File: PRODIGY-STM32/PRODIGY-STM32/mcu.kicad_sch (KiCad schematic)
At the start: 23 parts, among them U3 STM32F407VGTx, U4 M24C32-WMN6TP, Y2 8MHz, Y3 32.768kHz

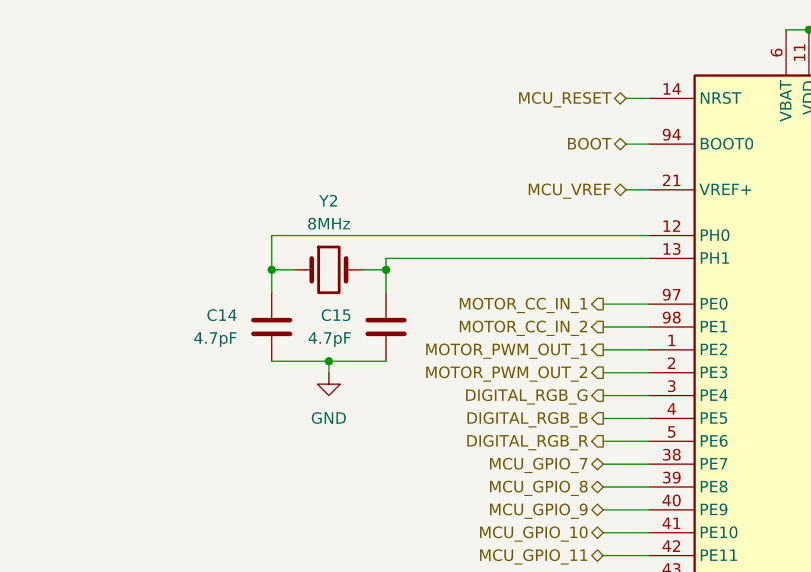
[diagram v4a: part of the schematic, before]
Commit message: stm32 started, footprints updated, lazout started
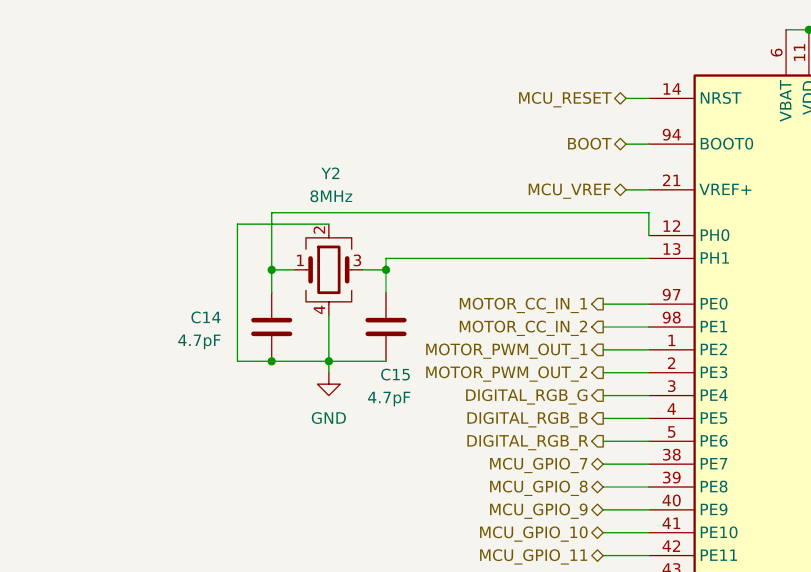
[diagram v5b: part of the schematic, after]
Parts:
- removed Y2: 8MHz, Crystal:Crystal_SMD_5032-4Pin_5.0x3.2mm, symbol Device:Crystal
- added Y2: 8MHz, Crystal:Crystal_SMD_5032-4Pin_5.0x3.2mm, symbol Device:Crystal_GND24
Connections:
- net GND: now also Y2.2, Y2.4
- net at C14.1, U3.12 (PH0): now also Y2.1
- net at C15.1, U3.13 (PH1): now also Y2.3
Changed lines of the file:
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@@
 	)
 	(junction
+		(at 59.69 60.96)
+		(diameter 0)
+		(color 0 0 0 0)
+	)
+	(junction
 		(at 224.79 62.23)
 		(diameter 0)
@@
 	(wire
 		(pts
-			(xy 59.69 46.99) (xy 101.6 46.99)
+			(xy 59.69 44.45) (xy 101.6 44.45)
 		)
 		(stroke
@@
 	(wire
 		(pts
+			(xy 55.88 60.96) (xy 59.69 60.96)
+		)
+		(stroke
+			(width 0)
+			(type default)
+		)
+	)
+	(wire
+		(pts
 			(xy 124.46 20.32) (xy 124.46 24.13)
 		)
@@
 	(wire
 		(pts
+			(xy 66.04 55.88) (xy 66.04 60.96)
+		)
+		(stroke
+			(width 0)
+			(type default)
+		)
+	)
+	(wire
+		(pts
 			(xy 157.48 167.64) (xy 151.13 167.64)
 		)
@@
 	(wire
 		(pts
+			(xy 101.6 44.45) (xy 101.6 46.99)
+		)
+		(stroke
+			(width 0)
+			(type default)
+		)
+	)
+	(wire
+		(pts
 			(xy 151.13 80.01) (xy 147.32 80.01)
 		)
@@
 	(wire
 		(pts
-			(xy 59.69 50.8) (xy 59.69 46.99)
+			(xy 59.69 50.8) (xy 59.69 44.45)
 		)
 		(stroke
@@
 	(wire
 		(pts
+			(xy 55.88 45.72) (xy 55.88 60.96)
+		)
+		(stroke
+			(width 0)
+			(type default)
+		)
+	)
+	(wire
+		(pts
 			(xy 96.52 59.69) (xy 101.6 59.69)
 		)
@@
 	(wire
 		(pts
+			(xy 66.04 45.72) (xy 55.88 45.72)
+		)
+		(stroke
+			(width 0)
+			(type default)
+		)
+	)
+	(wire
+		(pts
 			(xy 46.99 171.45) (xy 54.61 171.45)
 		)
@@
 		(dnp no)
 		(property "Reference" "C14"
-			(at 55.88 55.8799 0)
+			(at 54.102 56.134 0)
 			(effects
 				(font
@@
 		)
 		(property "Value" "4.7pF"
-			(at 55.88 58.4199 0)
+			(at 54.102 58.674 0)
 			(effects
 				(font
@@
 		)
 		(instances
-			(project ""
+			(project "PRODIGY-STM32"
 				(path "/f2f1c781-b8fe-416b-b7a0-b424640c1d9f/2c940864-b0c7-4fea-a950-c583ebb4a87f"
 					(reference "U3")
@@
 	)
 	(symbol
-		(lib_id "Device:Crystal")
-		(at 66.04 50.8 0)
-		(unit 1)
-		(exclude_from_sim no)
-		(in_bom yes)
-		(on_board yes)
-		(dnp no)
-		(fields_autoplaced yes)
-		(property "Reference" "Y2"
-			(at 66.04 43.18 0)
-			(effects
-				(font
-					(size 1.27 1.27)
-				)
-			)
-		)
-		(property "Value" "8MHz"
-			(at 66.04 45.72 0)
-			(effects
-				(font
-					(size 1.27 1.27)
-				)
-			)
-		)
-		(property "Footprint" "Crystal:Crystal_SMD_5032-4Pin_5.0x3.2mm"
-			(at 66.04 50.8 0)
-			(effects
-				(font
-					(size 1.27 1.27)
-				)
-				(hide yes)
-			)
-		)
-		(property "Datasheet" "~"
-			(at 66.04 50.8 0)
-			(effects
-				(font
-					(size 1.27 1.27)
-				)
-				(hide yes)
-			)
-		)
-		(property "Description" "Two pin crystal"
-			(at 66.04 50.8 0)
-			(effects
-				(font
-					(size 1.27 1.27)
-				)
-				(hide yes)
-			)
-		)
-		(property "MOUSER" ""
-			(at 66.04 50.8 0)
-			(effects
-				(font
-					(size 1.27 1.27)
-				)
-				(hide yes)
-			)
-		)
-		(property "TME" "8.00M-CFPX104"
-			(at 66.04 50.8 0)
-			(effects
-				(font
-					(size 1.27 1.27)
-				)
-				(hide yes)
-			)
-		)
-		(pin "1"
-		)
-		(pin "2"
-		)
-		(instances
-			(project "PRODIGY-STM32"
-				(path "/f2f1c781-b8fe-416b-b7a0-b424640c1d9f/2c940864-b0c7-4fea-a950-c583ebb4a87f"
-					(reference "Y2")
-					(unit 1)
-				)
-			)
-		)
-	)
-	(symbol
 		(lib_id "power:+3V3")
 		(at 259.08 27.94 0)
@@
 		)
 		(instances
-			(project ""
+			(project "PRODIGY-STM32"
 				(path "/f2f1c781-b8fe-416b-b7a0-b424640c1d9f/2c940864-b0c7-4fea-a950-c583ebb4a87f"
 					(reference "U4")
@@
 	)
 	(symbol
+		(lib_id "Device:Crystal_GND24")
+		(at 66.04 50.8 0)
+		(unit 1)
+		(exclude_from_sim no)
+		(in_bom yes)
+		(on_board yes)
+		(dnp no)
+		(property "Reference" "Y2"
+			(at 66.294 40.132 0)
+			(effects
+				(font
+					(size 1.27 1.27)
+				)
+			)
+		)
+		(property "Value" "8MHz"
+			(at 66.294 42.672 0)
+			(effects
+				(font
+					(size 1.27 1.27)
+				)
+			)
+		)
+		(property "Footprint" "Crystal:Crystal_SMD_5032-4Pin_5.0x3.2mm"
+			(at 66.04 50.8 0)
+			(effects
+				(font
+					(size 1.27 1.27)
+				)
+				(hide yes)
+			)
+		)
+		(property "Datasheet" "~"
+			(at 66.04 50.8 0)
+			(effects
+				(font
+					(size 1.27 1.27)
+				)
+				(hide yes)
+			)
+		)
+		(property "Description" "Four pin crystal, GND on pins 2 and 4"
+			(at 66.04 50.8 0)
+			(effects
+				(font
+					(size 1.27 1.27)
+				)
+				(hide yes)
+			)
+		)
+		(property "TME" "8.00M-CFPX104"
+			(at 66.04 50.8 0)
+			(effects
+				(font
+					(size 1.27 1.27)
+				)
+				(hide yes)
+			)
+		)
+		(pin "4"
+		)
+		(pin "1"
+		)
+		(pin "2"
+		)
+		(pin "3"
+		)
+		(instances
+			(project "PRODIGY-STM32"
+				(path "/f2f1c781-b8fe-416b-b7a0-b424640c1d9f/2c940864-b0c7-4fea-a950-c583ebb4a87f"
+					(reference "Y2")
+					(unit 1)
+				)
+			)
+		)
+	)
+	(symbol
 		(lib_id "Device:C")
 		(at 72.39 57.15 0)
@@
 		(dnp no)
 		(property "Reference" "C15"
-			(at 68.58 55.8799 0)
+			(at 75.184 62.484 0)
 			(effects
 				(font
@@
 		)
 		(property "Value" "4.7pF"
-			(at 68.58 58.4199 0)
+			(at 75.184 65.024 0)
 			(effects
 				(font
